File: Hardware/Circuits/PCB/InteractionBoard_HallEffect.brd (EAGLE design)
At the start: 72.1 x 146.3 mm, 70 parts, among them J3 F-2X10-DIL-2MM, SW1 219-10, U1 DRV5032FADBZRDBZ0003A_L, U2 SX1509, U3 DRV5032FADBZRDBZ0003A_L, U4 DRV5032FADBZRDBZ0003A_L, U5 DRV5032FADBZRDBZ0003A_L, U6 DRV5032FADBZRDBZ0003A_L, U7 DRV5032FADBZRDBZ0003A_L, U8 DRV5032FADBZRDBZ0003A_L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

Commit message: manually routed
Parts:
- removed JP1: JUMPER-SMT_3_1-NC_TRACE_NO-SILK, SparkFun-Jumpers:SMT-JUMPER_3_1-NC_TRACE_NO-SILK
- removed S2: (no value), SparkFun-Switches:TACTILE_SWITCH_SMD_5.2MM
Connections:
- net 3.3V: no longer S2.1, S2.2
- net 4_SX3: no longer JP1.1
- net GND_MCU: no longer RN2.3
- net RESET: no longer JP1.2, JP1.3, RN2.6, S2.3, S2.4
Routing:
- net GND_MCU: track 601.2 -> 144.2 mm, vias 14 -> 18
- net 3.3V: track 749.4 -> 511.3 mm, vias 14 -> 20
- net RESET: track 56.3 -> 0.00 mm, vias 3 -> 0
- net NEOPIXEL_07: track 53.7 -> 101.3 mm, vias 2 -> 5
- net 4_SX3: track 45.8 -> 0.00 mm, vias 4 -> 0
- net VCC_5V: track 415.8 -> 382.2 mm, vias 10 -> 4
- net SCL_00: track 188.4 -> 156.0 mm
- net 2_SX2: track 47.7 -> 68.8 mm
- net INT_03: track 74.2 -> 94.0 mm, vias 4 -> 11
- net 3_SX2: track 47.9 -> 63.9 mm
- net 4_SX2: track 54.4 -> 68.1 mm, vias 4 -> 2
- net SDA_00: track 181.0 -> 167.7 mm, vias 4 -> 8
- net 7_SX2: track 47.2 -> 60.1 mm
- net INT_01: track 115.6 -> 104.1 mm
- net NEOPIXEL_01: track 126.8 -> 115.9 mm
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
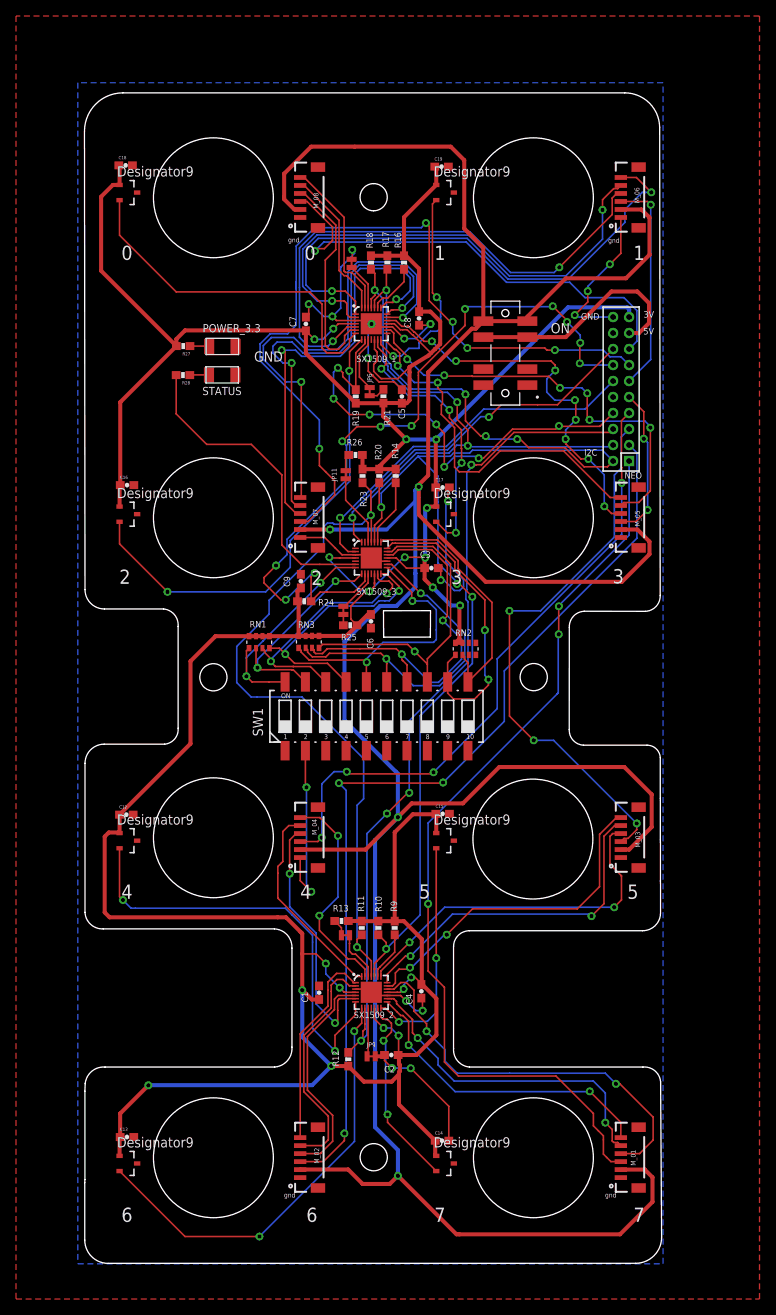
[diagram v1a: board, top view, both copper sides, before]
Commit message: less unused space
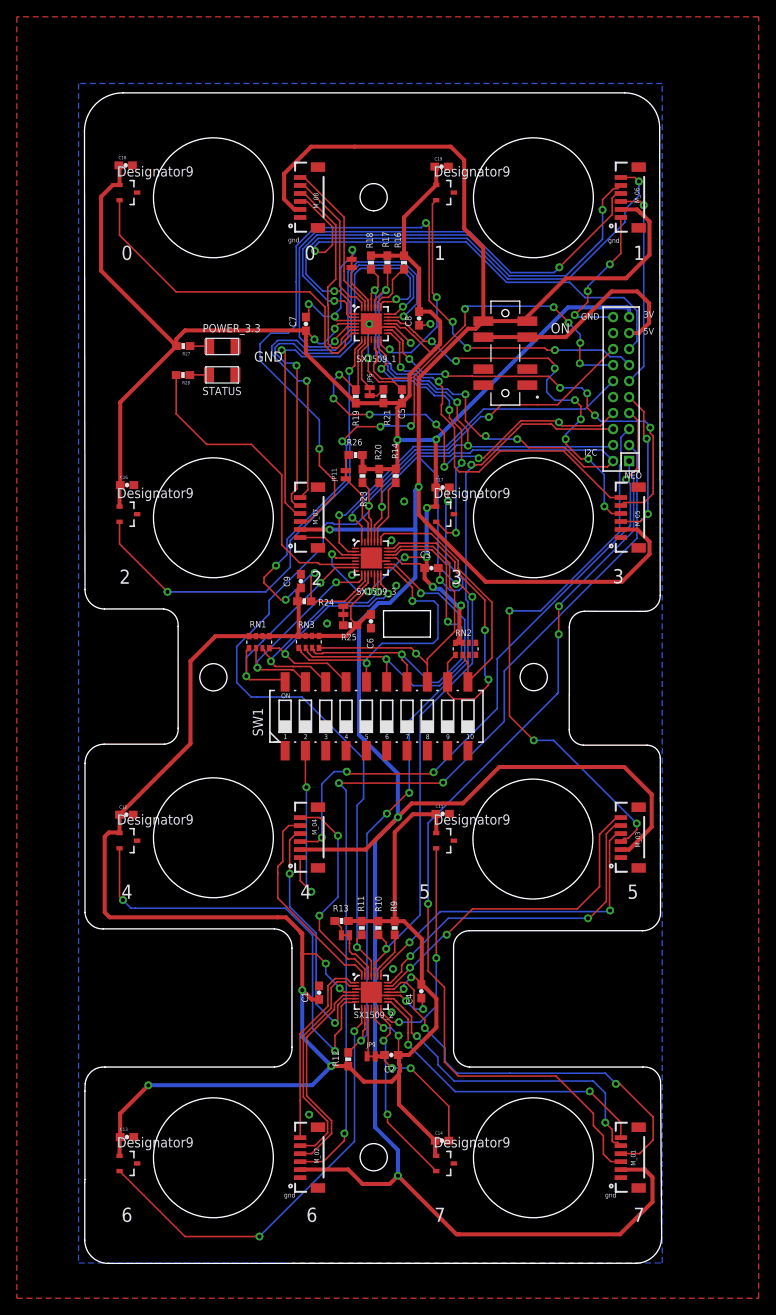
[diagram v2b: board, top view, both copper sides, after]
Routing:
- net VCC_5V: track 382.2 -> 376.9 mm
- net NEOPIXEL_04: track 79.5 -> 82.6 mm
- net 2_SX2: track 68.8 -> 65.9 mm
- net 8_SX3: track 32.4 -> 29.8 mm
- net 9_SX3: track 32.6 -> 30.5 mm
- net 9_SX2: track 27.6 -> 25.7 mm
- net 13_SX2: track 60.5 -> 58.8 mm
- net 15_SX1: track 44.5 -> 43.0 mm
- net INT_02: track 58.9 -> 57.4 mm
- net 3.3V: track 511.3 -> 509.9 mm
- net 10_SX3: track 34.7 -> 36.0 mm
- net NEOPIXEL_06: track 27.1 -> 25.8 mm
- net GND_MCU: track 144.2 -> 143.0 mm, vias 18 -> 26
- net 15_SX3: track 32.7 -> 33.7 mm
- net 4_SX1: track 28.0 -> 27.0 mm
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
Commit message: connected ground
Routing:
- net GND_MCU: track 143.0 -> 147.9 mm, vias 26 -> 24
- net VCC_5V: track 376.9 -> 379.0 mm
- net 7_SX2: track 60.1 -> 61.0 mm
- net SDA_00: track 168.6 -> 169.5 mm
- net 1_SX3: track 45.3 -> 46.1 mm
- net 7_SX3: track 28.1 -> 27.4 mm
- net 3.3V: track 509.9 -> 510.4 mm
